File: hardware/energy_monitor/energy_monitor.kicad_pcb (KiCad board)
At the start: 4 copper layers, 102.8 x 86.9 mm, 139 parts, among them J1 Screw_Terminal_01x03, J2 Screw_Terminal_01x04, J3 Screw_Terminal_01x04, J4 Screw_Terminal_01x04, J5 USB_OTG, Q1 MMBT2222, Q2 MMBT2222, U1 RAC04, U2 TPS730, U3 TPS723, U4 ADS131E08, U5 AP2112, U6 CP2104, U7 ESP-WROOM-32U, U8 ISO7421, U9 ISO7420

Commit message: Working on layout
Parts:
- moved C41 75.0 mm to (151.9, 73.5), turned to 90 degrees
- moved C40 72.7 mm to (150.2, 73.1), turned to 90 degrees
- moved C37 68.0 mm to (145.7, 85.5), turned to 180 degrees
- moved C39 65.0 mm to (146.1, 83.8), turned to 180 degrees
- moved C32 54.4 mm to (165.3, 83.5)
- moved C43 52.4 mm to (165.6, 81.8)
- moved C36 52.0 mm to (165.2, 86.9)
- moved C48 50.7 mm to (165.6, 77.6)
- moved C31 48.7 mm to (165.6, 85.2)
- moved C49 45.3 mm to (166.1, 79.7)
- moved C34 43.3 mm to (165.6, 88.6)
- moved U7 6.54 mm to (182.7, 62.3), turned to 90 degrees
- moved C13 4.70 mm to (134.5, 57.0)
- moved U4 2.85 mm to (155.7, 83.1)
- moved C44 2.33 mm to (145.7, 80.6)
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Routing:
- net /I1_P: track 5.76 -> 45.4 mm
- net /I1_N: track 5.79 -> 45.4 mm
- net /I6_N: track 5.76 -> 40.2 mm
- net /I6_P: track 5.76 -> 40.2 mm
- net /L1_P: track 0.00 -> 32.4 mm
- net /L1_N: track 0.00 -> 31.7 mm
- net /I2_N: track 5.76 -> 36.2 mm
- net /I2_P: track 5.76 -> 36.2 mm
- net /L2_P: track 0.00 -> 27.4 mm
- net /L2_N: track 0.00 -> 26.7 mm
- net /I5_N: track 5.76 -> 31.0 mm
- net /I5_P: track 5.76 -> 31.0 mm
- net /I3_P: track 5.76 -> 20.5 mm
- net /I3_N: track 5.76 -> 20.5 mm
- net GNDA: track 171.7 -> 183.5 mm
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
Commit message: Working on layout
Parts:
- moved U8 46.8 mm to (181.8, 60.0), turned to 270 degrees
- moved U5 40.3 mm to (143.2, 53.2)
- moved U9 37.7 mm to (188.2, 60.0), turned to 270 degrees
- moved C42 37.2 mm to (146.3, 53.2), turned to 270 degrees
- moved U6 31.7 mm to (183.6, 50.2), turned to 270 degrees
- moved C38 31.0 mm to (140.3, 53.2), turned to 270 degrees
- moved D23 25.5 mm to (207.3, 79.8)
- moved D24 25.5 mm to (215.9, 83.8)
- moved R31 25.5 mm to (205.8, 83.6)
- moved R32 25.5 mm to (217.2, 80.2)
- moved U7 20.6 mm to (163.0, 56.4), turned to 180 degrees
- moved J5 20.4 mm to (179.1, 33.1)
- moved C41 8.00 mm to (146.1, 78.9), turned to 180 degrees
- moved C40 6.09 mm to (145.7, 77.2), turned to 180 degrees
- moved U2 3.00 mm to (143.2, 59.7)
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
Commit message: Working on layout
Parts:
- moved D24 74.5 mm to (158.0, 37.0), turned to 270 degrees
- moved R32 71.6 mm to (158.0, 40.0), turned to 90 degrees
- moved D23 67.6 mm to (155.0, 37.0), turned to 270 degrees
- moved R31 66.9 mm to (155.0, 40.0), turned to 90 degrees
- moved C51 57.1 mm to (150.1, 54.5), turned to 270 degrees
- moved R35 56.2 mm to (150.1, 51.9), turned to 90 degrees
- moved C56 50.6 mm to (190.2, 71.3)
- moved Q2 48.3 mm to (187.0, 76.1)
- moved R34 48.0 mm to (183.9, 75.1), turned to 180 degrees
- moved C55 45.6 mm to (183.3, 71.3)
- moved R33 44.0 mm to (183.9, 77.1)
- moved Q1 43.6 mm to (180.8, 76.1), turned to 180 degrees
- moved C54 40.6 mm to (190.2, 61.9)
- moved C53 38.5 mm to (183.3, 61.9)
- moved C47 36.0 mm to (183.2, 58.8), turned to 180 degrees
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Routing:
- net Net-(D25-Pad1): track 0.00 -> 41.1 mm, vias 0 -> 2
- net Net-(D26-Pad1): track 0.00 -> 36.6 mm, vias 0 -> 2
- net Net-(U6-Pad21): track 0.00 -> 19.0 mm, vias 0 -> 2
- net /VUSB: track 0.00 -> 17.9 mm, vias 0 -> 2
- net Net-(U6-Pad20): track 0.00 -> 15.9 mm
- net /D_P: track 0.00 -> 15.2 mm, vias 0 -> 2
- net Net-(U6-Pad23): track 0.00 -> 13.6 mm
- net /D_N: track 0.00 -> 13.5 mm
- net VCC: track 0.00 -> 13.2 mm, vias 0 -> 5
- net GND: track 0.00 -> 13.0 mm, vias 0 -> 14
- net Net-(U6-Pad19): track 0.00 -> 12.1 mm, vias 0 -> 2
- net GNDA: track 183.5 -> 194.9 mm, vias 0 -> 12
- net +2.5V: track 5.28 -> 8.70 mm, vias 0 -> 1
- net -2.5V: track 4.96 -> 8.38 mm, vias 0 -> 1
- net Net-(C47-Pad1): track 0.00 -> 2.57 mm
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- added copper zone on In2.Cu, net +2.5V
- added copper zone on In1.Cu, net GND
- added copper zone on In2.Cu, net VCC

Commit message: Working on layout
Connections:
- net /DRDY renamed /ADC_DRDY
- net /PWDN renamed /ADC_PWDN
- net /START renamed /ADC_START
- U4 pad 36: /RESET -> /ADC_RESET
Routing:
- net -2.5V: track 8.38 -> 43.8 mm, vias 1 -> 31
- net +2.5V: track 8.70 -> 35.7 mm, vias 1 -> 23
- net GNDA: track 194.9 -> 207.7 mm, vias 12 -> 22
- added copper zone on B.Cu, net -2.5V

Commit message: Working on layout
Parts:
- moved Q1 0.40 mm to (180.8, 75.7)
- moved Q2 0.40 mm to (187.0, 75.7)
- moved R33 0.40 mm to (183.9, 76.7)
- moved R34 0.40 mm to (183.9, 74.7)
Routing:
- net /RESET: track 0.00 -> 42.5 mm
- net /TXD0: track 0.00 -> 27.0 mm, vias 0 -> 2
- net /RXD0: track 0.00 -> 25.6 mm
- net /GPIO0: track 0.00 -> 22.4 mm, vias 0 -> 2
- net /CS: track 0.00 -> 18.0 mm, vias 0 -> 2
- net /MISO: track 0.00 -> 12.9 mm
- net /SCK: track 0.00 -> 12.9 mm
- net /DTR: track 0.00 -> 9.63 mm
- net /RTS: track 0.00 -> 9.25 mm
- net /MOSI: track 0.00 -> 8.50 mm
- net +3V3: track 5.33 -> 11.6 mm, vias 0 -> 2
- net GNDA: track 207.7 -> 213.0 mm, vias 22 -> 26
- net Net-(Q2-Pad1): track 0.00 -> 1.37 mm
- net Net-(Q1-Pad1): track 0.00 -> 1.37 mm
- added copper zone on In2.Cu, net +3V3

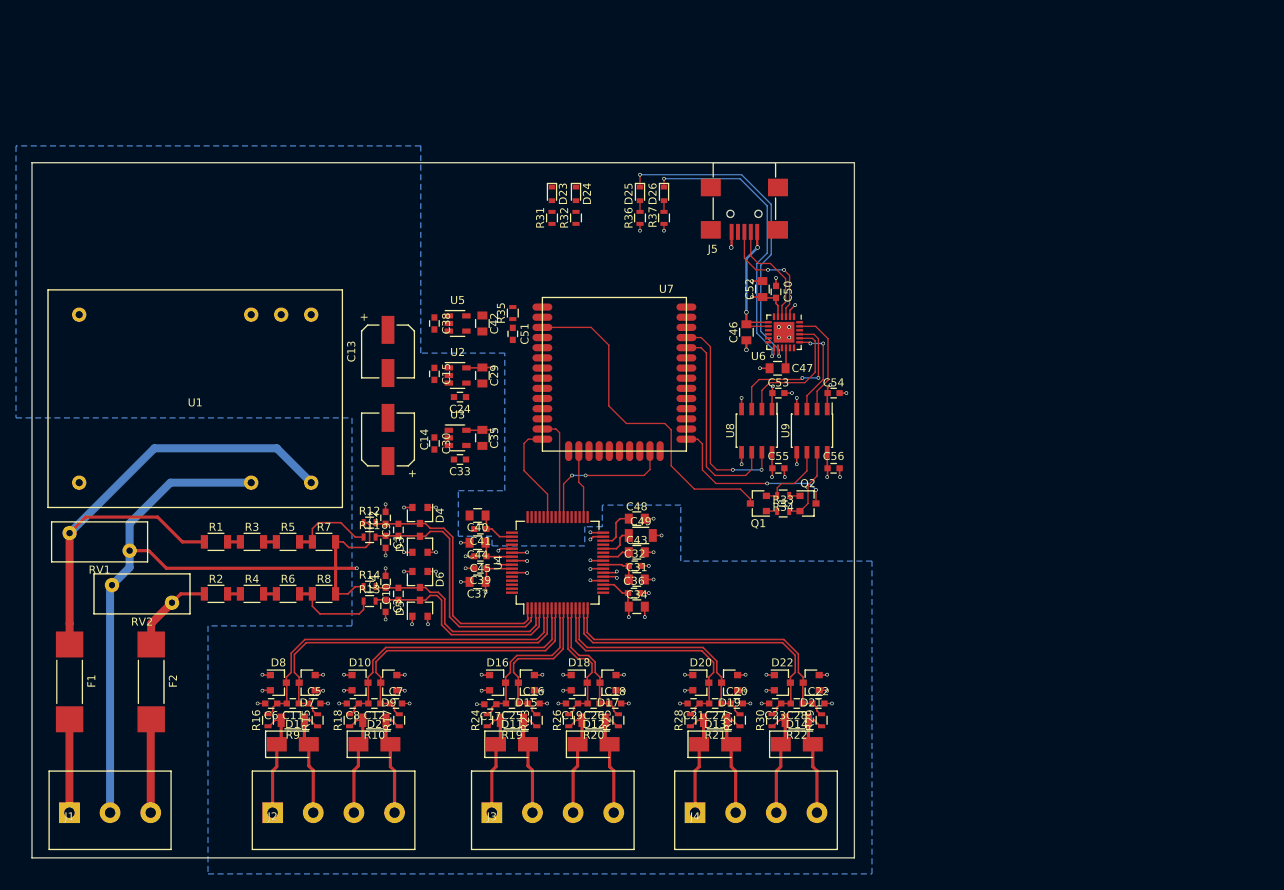
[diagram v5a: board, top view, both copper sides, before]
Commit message: Finished routing board
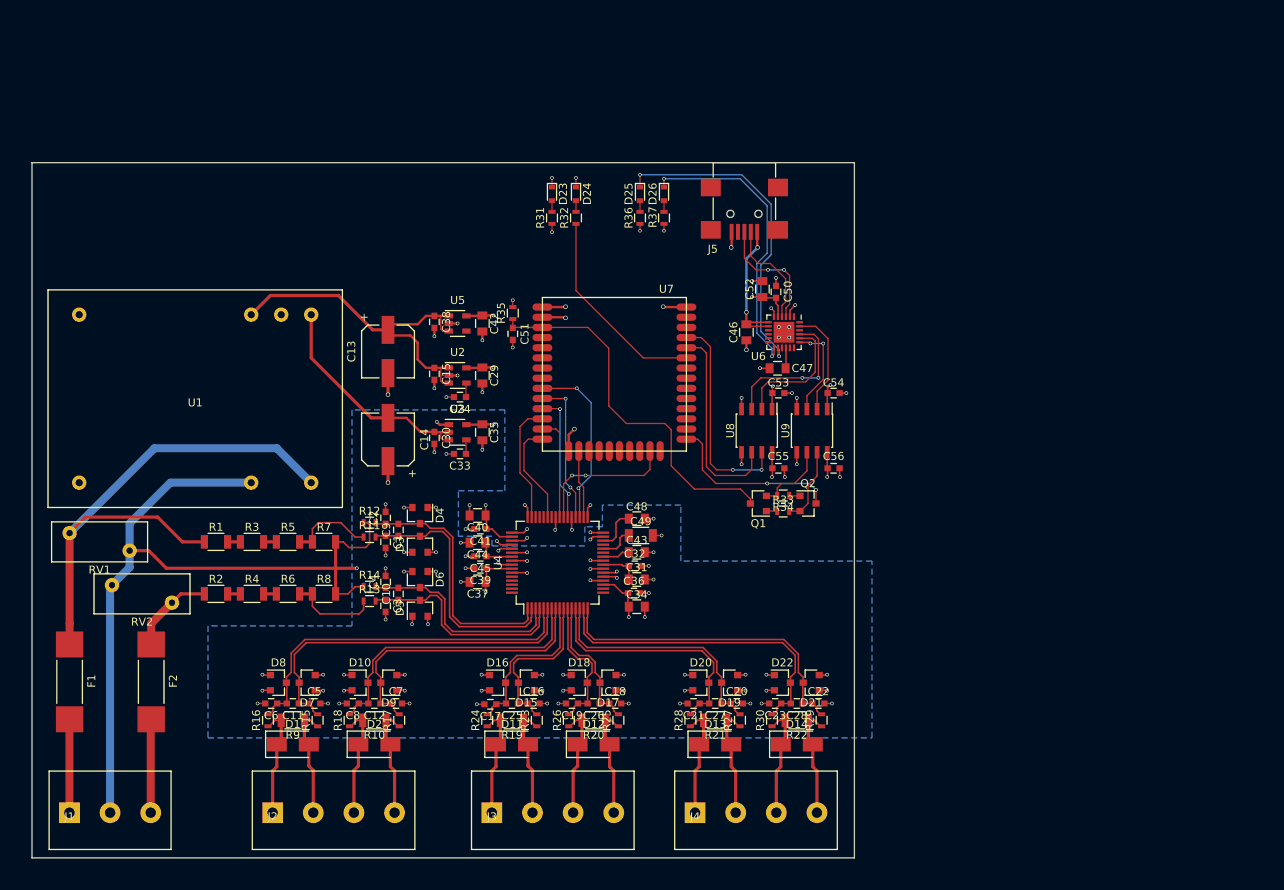
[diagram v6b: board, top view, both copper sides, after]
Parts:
- moved C30 0.70 mm to (140.3, 67.5)
- moved C33 0.70 mm to (143.5, 69.5)
- moved C35 0.70 mm to (146.3, 66.8)
- moved U3 0.70 mm to (143.2, 66.8)
- moved C38 0.20 mm to (140.3, 53.0)
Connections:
- U7 pad 10: Net-(U7-Pad10) -> /ADC_RESET
- U7 pad 11: Net-(U7-Pad11) -> /ADC_START
- U7 pad 12: Net-(U7-Pad12) -> /ADC_DRDY
- U7 pad 33: Net-(U7-Pad33) -> /LED
- U7 pad 9: Net-(U7-Pad9) -> /ADC_PWDN
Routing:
- net +5V: track 0.00 -> 44.5 mm
- net GNDA: track 213.0 -> 254.2 mm, vias 26 -> 52
- net -5V: track 0.00 -> 28.3 mm
- net /LED: track 0.00 -> 25.6 mm
- net /ADC_PWDN: track 0.00 -> 21.9 mm, vias 0 -> 2
- net /ADC_RESET: track 0.00 -> 18.2 mm, vias 0 -> 2
- net /ADC_START: track 0.00 -> 16.2 mm, vias 0 -> 2
- net /ADC_DRDY: track 0.00 -> 15.1 mm
- net +3V3: track 11.6 -> 24.9 mm, vias 2 -> 9
- net /RESET: track 42.5 -> 47.1 mm
- net Net-(C33-Pad1): track 0.00 -> 1.77 mm
- net Net-(C24-Pad1): track 0.00 -> 1.77 mm
- net Net-(D24-Pad2): track 0.00 -> 1.40 mm
- net Net-(D23-Pad2): track 0.00 -> 1.40 mm
- net VCC: track 13.2 -> 14.4 mm, vias 5 -> 6

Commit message: Fixed silkscreen layers
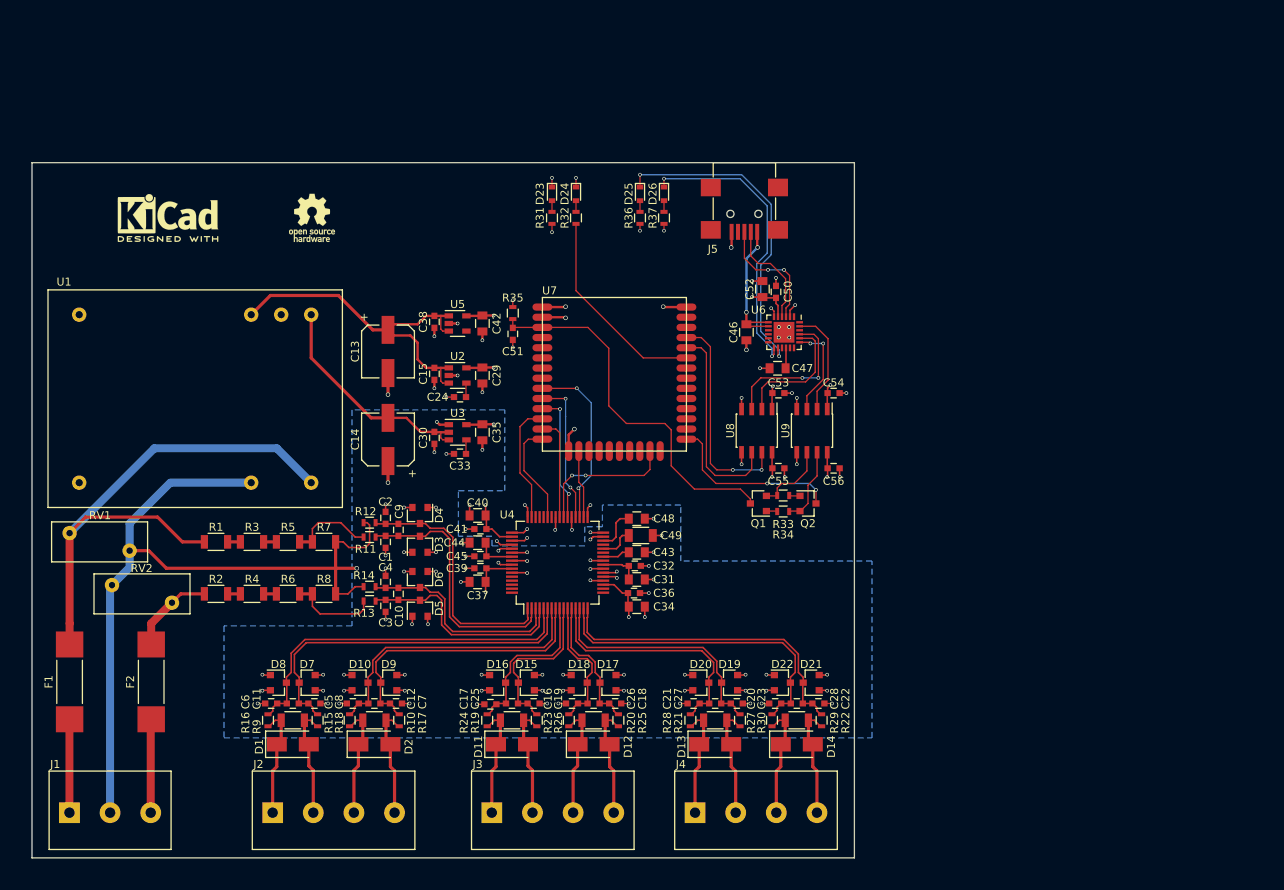
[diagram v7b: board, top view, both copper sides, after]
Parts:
- added REF***: KiCad-Logo_12mm_SilkScreen, Symbols:KiCad-Logo2_6mm_SilkScreen, F.Cu at (107.0, 40.0)
- added REF***: OSHW-Logo_5.7x6mm_SilkScreen, Symbols:OSHW-Logo_5.7x6mm_SilkScreen, F.Cu at (125.0, 40.0)
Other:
- rule pad_to_mask_clearance: 0.2 -> 0.05

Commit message: Added 2 more LEDs.  Added labels to LEDs.  Added board rev #
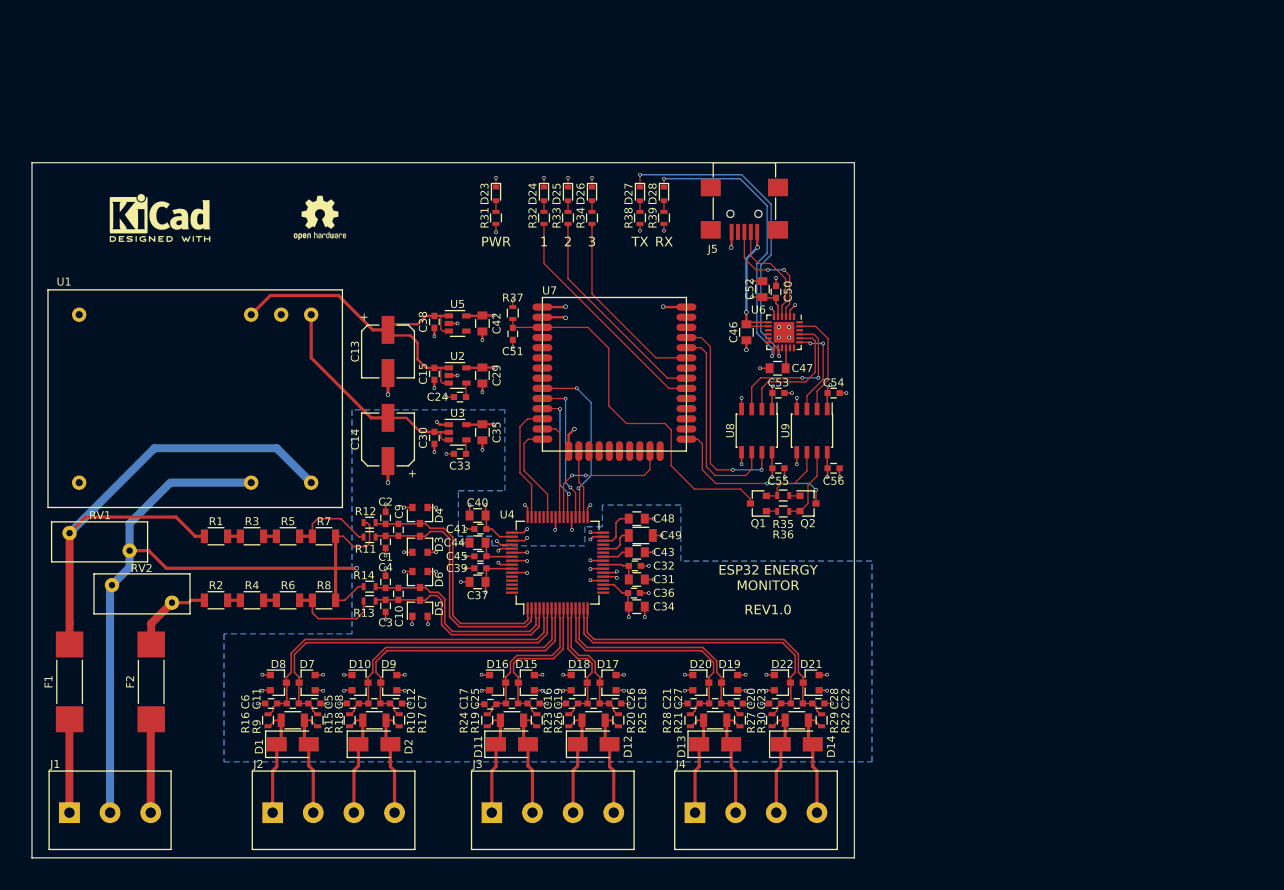
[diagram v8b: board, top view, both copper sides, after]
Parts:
- removed the REF*** at (125.0, 40.0)
- added D25: GRN, Diodes_SMD:D_0603, F.Cu at (157.0, 37.0)
- added D26: GRN, Diodes_SMD:D_0603, F.Cu at (160.0, 37.0)
- added R33: 1k, Resistors_SMD:R_0603, F.Cu at (157.0, 40.0)
- added R34: 1k, Resistors_SMD:R_0603, F.Cu at (160.0, 40.0)
- added REF***: OSHW-Logo2_7.3x6mm_SilkScreen, Symbols:OSHW-Logo2_7.3x6mm_SilkScreen, F.Cu at (126.0, 40.0)
- REF***: value KiCad-Logo_12mm_SilkScreen -> KiCad-Logo2_6mm_SilkScreen
- moved D23 7.00 mm to (148.0, 37.0)
- moved R31 7.00 mm to (148.0, 40.0)
- moved D24 4.00 mm to (154.0, 37.0)
- moved R32 4.00 mm to (154.0, 40.0)
- moved REF*** 1.00 mm to (106.0, 40.0)
- moved R2 0.80 mm to (113.0, 87.8)
- moved R4 0.80 mm to (117.5, 87.8)
- moved R6 0.80 mm to (122.0, 87.8)
- moved R8 0.80 mm to (126.5, 87.8)
- moved R1 0.70 mm to (113.0, 79.8)
- moved R3 0.70 mm to (117.5, 79.8)
- moved R5 0.70 mm to (122.0, 79.8)
- moved R7 0.70 mm to (126.5, 79.8)
- renumbered D25 to D27, D26 to D28, R33 to R35, R34 to R36, R35 to R37, R36 to R38, R37 to R39
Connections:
- R32 pad 1: /LED -> /LED1
- U7 pad 30: Net-(U7-Pad30) -> /LED1
- U7 pad 31: Net-(U7-Pad31) -> /LED2
- U7 pad 33: /LED -> /LED3
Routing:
- net /LED1: track 0.00 -> 29.2 mm
- net /LED2: track 0.00 -> 26.8 mm
- net /LED: track 25.6 -> 0.00 mm
- net /LED3: track 0.00 -> 23.9 mm
- net GNDA: track 254.2 -> 258.6 mm, vias 52 -> 54
- net Net-(D26-Pad2): track 0.00 -> 1.40 mm
- net Net-(D25-Pad2): track 0.00 -> 1.40 mm
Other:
- board text added: "1"
- board text added: "2"
- board text added: "3"
- board text added: "ESP32 ENERGY MONITOR"
- board text added: "PWR"
- board text added: "REV1.0"
- board text added: "RX"
- board text added: "TX"
